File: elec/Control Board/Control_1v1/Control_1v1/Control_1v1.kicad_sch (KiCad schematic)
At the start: 163 parts, among them J1 DB9_Female_MountingHoles, J10 Conn_02x12_Odd_Even, J11 Screw_Terminal_01x02, J14 Conn_01x10, J2 Conn_01x08, J25 Screw_Terminal_01x02, J26 Conn_01x10, J27 Conn_02x12_Odd_Even, J28 Screw_Terminal_01x02, J29 Conn_01x10, J3 Conn_01x08, J37 Conn_01x04, J4 Conn_01x08, J5 Conn_01x08, J6 Conn_01x08, J7 Conn_01x10, J8 Conn_02x18_Odd_Even, J9 Conn_01x10, Q601 BSS138

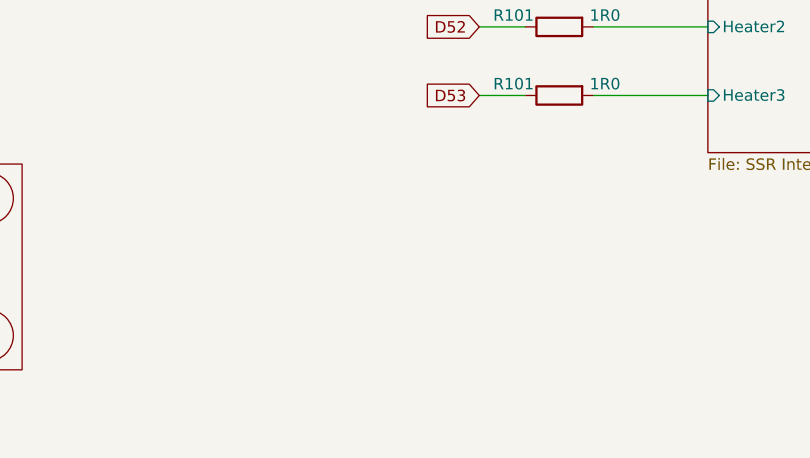
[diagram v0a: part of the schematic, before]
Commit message: Add Breadboard30P.
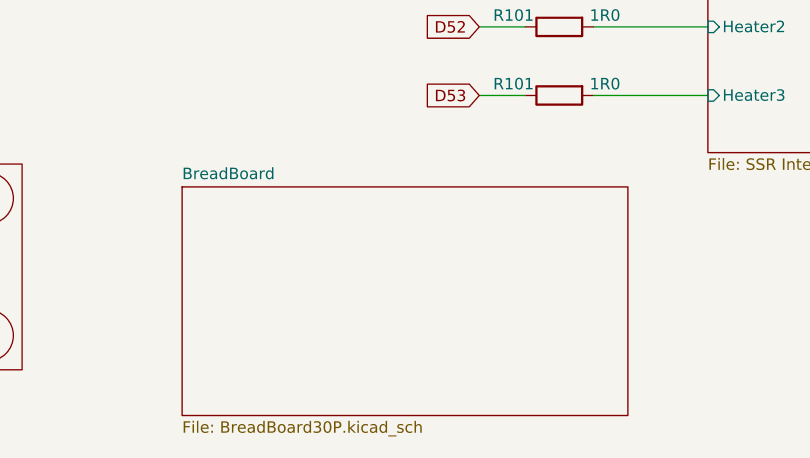
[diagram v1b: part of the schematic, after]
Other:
- added sheet BreadBoard (BreadBoard30P.kicad_sch)
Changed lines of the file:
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@@
+    )
+  )
+  (sheet (at 318.77 283.21) (size 49.53 25.4) (fields_autoplaced)
+    (stroke (width 0.1524) (type solid))
+    (fill (color 0 0 0 0.0000))
+    (property "Sheetname" "BreadBoard" (at 318.77 282.4984 0)
+      (effects (font (size 1.27 1.27)) (justify left bottom))
+    )
+    (property "Sheetfile" "BreadBoard30P.kicad_sch" (at 318.77 309.1946 0)
+      (effects (font (size 1.27 1.27)) (justify left top))
+    )
+    (instances
+      (project "Control_1v1"
+        (path "/c68c9deb-8d4d-42f0-adf8-4d3022f4ee59" (page "10"))
+      )
     )
   )

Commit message: Changes to change headders to sockets. Scockets for thermcouple amplifiers.
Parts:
- J14, J26, J29, J7, J9: Distributor 1 PN C2894933 -> C2905418
- J2, J3, J4, J5, J6: Distributor 1 PN C2894931 -> C2905417
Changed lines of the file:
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@@
       (effects (font (size 1.27 1.27)) hide)
     )
-    (property "Description" "3A Straight Square Pins 2.5mm 10P 6mm -40℃~+105℃ 3mm 2.54mm Plugin Black 1x10P Plugin,P=2.54mm Pin Headers ROHS" (at 419.1 50.8 0)
+    (property "Description" "2.54mm Plugin 3A 10P -40℃~+105℃ Straight 1x10P 8.5mm Top Square Holes Plugin,P=2.54mm Female Headers ROHS" (at 419.1 50.8 0)
       (effects (font (size 1.27 1.27)) hide)
     )
@@
       (effects (font (size 1.27 1.27)) hide)
     )
-    (property "Distributor 1 PN" "C2894933" (at 419.1 50.8 0)
+    (property "Distributor 1 PN" "C2905418" (at 419.1 50.8 0)
       (effects (font (size 1.27 1.27)) hide)
     )
@@
       (effects (font (size 1.27 1.27)) hide)
     )
-    (property "Description" "1x2P 20A -40℃~+105℃ 300V Green 12~30 Straight pin 5.08mm 2.5 1 2 Plugin,P=5.08mm Screw terminal ROHS" (at 471.17 203.2 0)
+    (property "Description" "1x2P XH 1 2.5mm 2 Brass Plugin,P=2.5mm Wire To Board / Wire To Wire Connector ROHS" (at 471.17 203.2 0)
       (effects (font (size 1.27 1.27)) hide)
     )
@@
       (effects (font (size 1.27 1.27)) hide)
     )
-    (property "Description" "3A Straight Square Pins 2.5mm 8P 6mm -40℃~+105℃ 3mm 2.54mm Plugin Black 1x8P Plugin,P=2.54mm Pin Headers ROHS" (at 171.45 165.1 0)
+    (property "Description" "2.54mm Plugin 3A 8P -40℃~+105℃ Straight 1x8P 8.5mm Top Square Holes Plugin,P=2.54mm Female Headers ROHS" (at 171.45 165.1 0)
       (effects (font (size 1.27 1.27)) hide)
     )
@@
       (effects (font (size 1.27 1.27)) hide)
     )
-    (property "Distributor 1 PN" "C2894931" (at 171.45 165.1 0)
+    (property "Distributor 1 PN" "C2905417" (at 171.45 165.1 0)
       (effects (font (size 1.27 1.27)) hide)
     )
@@
       (effects (font (size 1.27 1.27)) hide)
     )
-    (property "Description" "3A Straight Square Pins 2.5mm 8P 6mm -40℃~+105℃ 3mm 2.54mm Plugin Black 1x8P Plugin,P=2.54mm Pin Headers ROHS" (at 186.69 137.16 0)
+    (property "Description" "2.54mm Plugin 3A 8P -40℃~+105℃ Straight 1x8P 8.5mm Top Square Holes Plugin,P=2.54mm Female Headers ROHS" (at 186.69 137.16 0)
       (effects (font (size 1.27 1.27)) hide)
     )
@@
       (effects (font (size 1.27 1.27)) hide)
     )
-    (property "Distributor 1 PN" "C2894931" (at 186.69 137.16 0)
+    (property "Distributor 1 PN" "C2905417" (at 186.69 137.16 0)
       (effects (font (size 1.27 1.27)) hide)
     )
@@
       (effects (font (size 1.27 1.27)) hide)
     )
-    (property "Description" "3A Straight Square Pins 2.5mm 8P 6mm -40℃~+105℃ 3mm 2.54mm Plugin Black 1x8P Plugin,P=2.54mm Pin Headers ROHS" (at 160.02 76.2 0)
+    (property "Description" "2.54mm Plugin 3A 8P -40℃~+105℃ Straight 1x8P 8.5mm Top Square Holes Plugin,P=2.54mm Female Headers ROHS" (at 160.02 76.2 0)
       (effects (font (size 1.27 1.27)) hide)
     )
@@
       (effects (font (size 1.27 1.27)) hide)
     )
-    (property "Distributor 1 PN" "C2894931" (at 160.02 76.2 0)
+    (property "Distributor 1 PN" "C2905417" (at 160.02 76.2 0)
       (effects (font (size 1.27 1.27)) hide)
     )
@@
       (effects (font (size 1.27 1.27)) hide)
     )
-    (property "Description" "3A Straight Square Pins 2.5mm 8P 6mm -40℃~+105℃ 3mm 2.54mm Plugin Black 1x8P Plugin,P=2.54mm Pin Headers ROHS" (at 194.31 116.84 0)
+    (property "Description" "2.54mm Plugin 3A 8P -40℃~+105℃ Straight 1x8P 8.5mm Top Square Holes Plugin,P=2.54mm Female Headers ROHS" (at 194.31 116.84 0)
       (effects (font (size 1.27 1.27)) hide)
     )
@@
       (effects (font (size 1.27 1.27)) hide)
     )
-    (property "Distributor 1 PN" "C2894931" (at 194.31 116.84 0)
+    (property "Distributor 1 PN" "C2905417" (at 194.31 116.84 0)
       (effects (font (size 1.27 1.27)) hide)
     )
@@
       (effects (font (size 1.27 1.27)) hide)
     )
-    (property "Description" "3A Straight Square Pins 2.5mm 10P 6mm -40℃~+105℃ 3mm 2.54mm Plugin Black 1x10P Plugin,P=2.54mm Pin Headers ROHS" (at 482.6 121.92 0)
+    (property "Description" "2.54mm Plugin 3A 10P -40℃~+105℃ Straight 1x10P 8.5mm Top Square Holes Plugin,P=2.54mm Female Headers ROHS" (at 482.6 121.92 0)
       (effects (font (size 1.27 1.27)) hide)
     )
@@
       (effects (font (size 1.27 1.27)) hide)
     )
-    (property "Distributor 1 PN" "C2894933" (at 482.6 121.92 0)
+    (property "Distributor 1 PN" "C2905418" (at 482.6 121.92 0)
       (effects (font (size 1.27 1.27)) hide)
     )
@@
       (effects (font (size 1.27 1.27)) hide)
     )
-    (property "Description" "1x2P 20A -40℃~+105℃ 300V Green 12~30 Straight pin 5.08mm 2.5 1 2 Plugin,P=5.08mm Screw terminal ROHS" (at 471.17 168.91 0)
+    (property "Description" "1x2P XH 1 2.5mm 2 Brass Plugin,P=2.5mm Wire To Board / Wire To Wire Connector ROHS" (at 471.17 168.91 0)
       (effects (font (size 1.27 1.27)) hide)
     )
@@
       (effects (font (size 1.27 1.27)) hide)
     )
-    (property "Description" "3A Straight Square Pins 2.5mm 10P 6mm -40℃~+105℃ 3mm 2.54mm Plugin Black 1x10P Plugin,P=2.54mm Pin Headers ROHS" (at 482.6 50.8 0)
+    (property "Description" "2.54mm Plugin 3A 10P -40℃~+105℃ Straight 1x10P 8.5mm Top Square Holes Plugin,P=2.54mm Female Headers ROHS" (at 482.6 50.8 0)
       (effects (font (size 1.27 1.27)) hide)
     )
@@
       (effects (font (size 1.27 1.27)) hide)
     )
-    (property "Distributor 1 PN" "C2894933" (at 482.6 50.8 0)
+    (property "Distributor 1 PN" "C2905418" (at 482.6 50.8 0)
       (effects (font (size 1.27 1.27)) hide)
     )
@@
       (effects (font (size 1.27 1.27)) hide)
     )
-    (property "Description" "1x2P 20A -40℃~+105℃ 300V Green 12~30 Straight pin 5.08mm 2.5 1 2 Plugin,P=5.08mm Screw terminal ROHS" (at 482.6 21.59 0)
+    (property "Description" "1x2P XH 1 2.5mm 2 Brass Plugin,P=2.5mm Wire To Board / Wire To Wire Connector ROHS" (at 482.6 21.59 0)
       (effects (font (size 1.27 1.27)) hide)
     )
@@
       (effects (font (size 1.27 1.27)) hide)
     )
-    (property "Description" "3A Straight Square Pins 2.5mm 10P 6mm -40℃~+105℃ 3mm 2.54mm Plugin Black 1x10P Plugin,P=2.54mm Pin Headers ROHS" (at 345.44 91.44 0)
+    (property "Description" "2.54mm Plugin 3A 10P -40℃~+105℃ Straight 1x10P 8.5mm Top Square Holes Plugin,P=2.54mm Female Headers ROHS" (at 345.44 91.44 0)
       (effects (font (size 1.27 1.27)) hide)
     )
@@
       (effects (font (size 1.27 1.27)) hide)
     )
-    (property "Distributor 1 PN" "C2894933" (at 345.44 91.44 0)
+    (property "Distributor 1 PN" "C2905418" (at 345.44 91.44 0)
       (effects (font (size 1.27 1.27)) hide)
     )
@@
       (effects (font (size 1.27 1.27)) hide)
     )
-    (property "Description" "3A Straight Square Pins 2.5mm 8P 6mm -40℃~+105℃ 3mm 2.54mm Plugin Black 1x8P Plugin,P=2.54mm Pin Headers ROHS" (at 308.61 68.58 0)
+    (property "Description" "2.54mm Plugin 3A 8P -40℃~+105℃ Straight 1x8P 8.5mm Top Square Holes Plugin,P=2.54mm Female Headers ROHS" (at 308.61 68.58 0)
       (effects (font (size 1.27 1.27)) hide)
     )
@@
       (effects (font (size 1.27 1.27)) hide)
     )
-    (property "Distributor 1 PN" "C2894931" (at 308.61 68.58 0)
+    (property "Distributor 1 PN" "C2905417" (at 308.61 68.58 0)
       (effects (font (size 1.27 1.27)) hide)
     )
@@
       (effects (font (size 1.27 1.27)) hide)
     )
-    (property "Description" "3A Straight Square Pins 2.5mm 10P 6mm -40℃~+105℃ 3mm 2.54mm Plugin Black 1x10P Plugin,P=2.54mm Pin Headers ROHS" (at 419.1 121.92 0)
+    (property "Description" "2.54mm Plugin 3A 10P -40℃~+105℃ Straight 1x10P 8.5mm Top Square Holes Plugin,P=2.54mm Female Headers ROHS" (at 419.1 121.92 0)
       (effects (font (size 1.27 1.27)) hide)
     )
@@
       (effects (font (size 1.27 1.27)) hide)
     )
-    (property "Distributor 1 PN" "C2894933" (at 419.1 121.92 0)
+    (property "Distributor 1 PN" "C2905418" (at 419.1 121.92 0)
       (effects (font (size 1.27 1.27)) hide)
     )
@@
       (effects (font (size 1.27 1.27)) hide)
     )
-    (property "Description" "1x2P 20A -40℃~+105℃ 300V Green 12~30 Straight pin 5.08mm 2.5 1 2 Plugin,P=5.08mm Screw terminal ROHS" (at 482.6 92.71 0)
+    (property "Description" "1x2P XH 1 2.5mm 2 Brass Plugin,P=2.5mm Wire To Board / Wire To Wire Connector ROHS" (at 482.6 92.71 0)
       (effects (font (size 1.27 1.27)) hide)
     )
